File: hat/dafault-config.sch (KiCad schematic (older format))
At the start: 22 parts

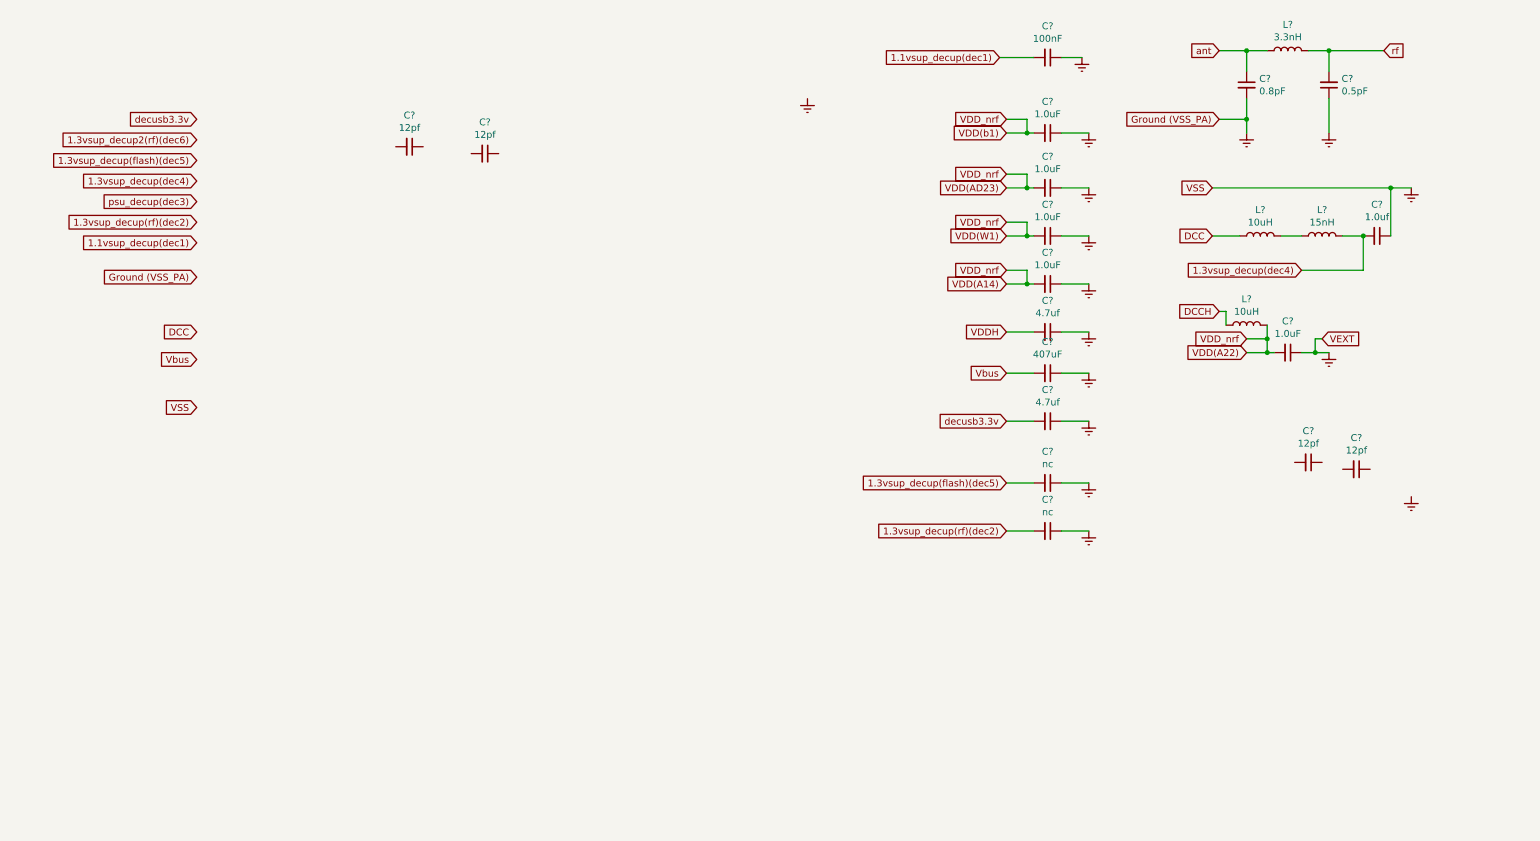
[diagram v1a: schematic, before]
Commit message: did some cleanup and added power connections
did some cleanup and added power connections
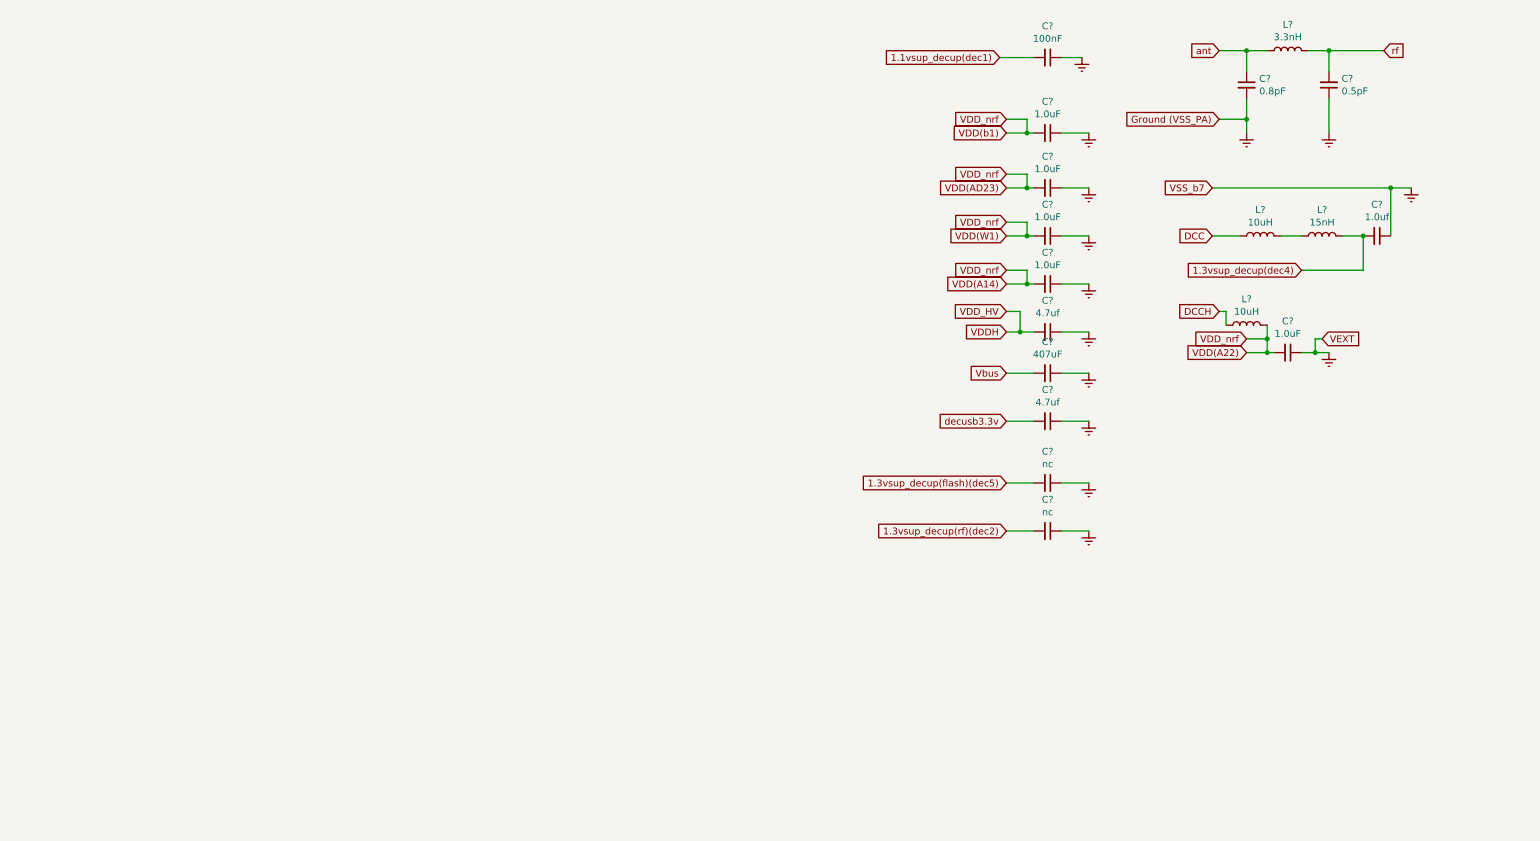
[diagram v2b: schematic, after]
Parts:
- removed C? (x4): 12pf, symbol Device:C_Small
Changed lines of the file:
@@
 Text GLabel 7900 1800 0    50   Input ~ 0
 VDD(AD23)
-Text GLabel 7900 2850 0    50   Input ~ 0
-VDDH
-Text GLabel 2000 3050 0    50   Input ~ 0
-Vbus
-Text GLabel 2000 2850 0    50   Input ~ 0
-DCC
+Text GLabel 7900 2700 0    50   Input ~ 0
+VDD_HV
 Text GLabel 9450 2700 0    50   Input ~ 0
 DCCH
-Text GLabel 2000 2450 0    50   Input ~ 0
-Ground (VSS_PA)
-Text GLabel 2000 2200 0    50   Input ~ 0
-1.1vsup_decup(dec1)
-Text GLabel 2000 2050 0    50   Input ~ 0
-1.3vsup_decup(rf)(dec2)
-Text GLabel 2000 1900 0    50   Input ~ 0
-psu_decup(dec3)
-Text GLabel 2000 1750 0    50   Input ~ 0
-1.3vsup_decup(dec4)
-Text GLabel 2000 1600 0    50   Input ~ 0
-1.3vsup_decup(flash)(dec5)
-Text GLabel 2000 1450 0    50   Input ~ 0
-1.3vsup_decup2(rf)(dec6)
-Text GLabel 2000 1300 0    50   Input ~ 0
-decusb3.3v
 $Comp
 L Device:C_Small C?
@@
 $Comp
 L Device:C_Small C?
-U 1 1 5CC155CD
-P 3550 1500
-AR Path="/5CC155CD" Ref="C?"  Part="1"
-AR Path="/5C9FDFE4/5CC155CD" Ref="C?"  Part="1"
-F 0 "C?" V 3321 1500 50  0000 C CNN
-F 1 "12pf" V 3412 1500 50  0000 C CNN
-F 2 "" H 3550 1500 50  0001 C CNN
-F 3 "~" H 3550 1500 50  0001 C CNN
-	1    3550 1500
-	0    1    1    0
-$EndComp
-$Comp
-L Device:C_Small C?
 U 1 1 5CC155E6
 P 8200 1400
@@
 F 3 "~" H 8200 1400 50  0001 C CNN
 	1    8200 1400
-	0    1    1    0
-$EndComp
-$Comp
-L Device:C_Small C?
-U 1 1 5CC155F4
-P 4100 1550
-AR Path="/5CC155F4" Ref="C?"  Part="1"
-AR Path="/5C9FDFE4/5CC155F4" Ref="C?"  Part="1"
-F 0 "C?" V 3871 1550 50  0000 C CNN
-F 1 "12pf" V 3962 1550 50  0000 C CNN
-F 2 "" H 4100 1550 50  0001 C CNN
-F 3 "~" H 4100 1550 50  0001 C CNN
-	1    4100 1550
 	0    1    1    0
 $EndComp
@@
 $Comp
 L Device:C_Small C?
-U 1 1 5CC1563E
-P 10100 3800
-AR Path="/5CC1563E" Ref="C?"  Part="1"
-AR Path="/5C9FDFE4/5CC1563E" Ref="C?"  Part="1"
-F 0 "C?" V 9871 3800 50  0000 C CNN
-F 1 "12pf" V 9962 3800 50  0000 C CNN
-F 2 "" H 10100 3800 50  0001 C CNN
-F 3 "~" H 10100 3800 50  0001 C CNN
-	1    10100 3800
-	0    1    1    0
-$EndComp
-$Comp
-L Device:C_Small C?
-U 1 1 5CC15651
-P 10450 3850
-AR Path="/5CC15651" Ref="C?"  Part="1"
-AR Path="/5C9FDFE4/5CC15651" Ref="C?"  Part="1"
-F 0 "C?" V 10221 3850 50  0000 C CNN
-F 1 "12pf" V 10312 3850 50  0000 C CNN
-F 2 "" H 10450 3850 50  0001 C CNN
-F 3 "~" H 10450 3850 50  0001 C CNN
-	1    10450 3850
-	0    1    1    0
-$EndComp
-$Comp
-L Device:C_Small C?
 U 1 1 5CC15663
 P 10600 2150
@@
 $EndComp
 $Comp
-L power:Earth #PWR?
+L power:Earth #PWR0101
 U 1 1 5CC15A29
 P 8450 850
-F 0 "#PWR?" H 8450 600 50  0001 C CNN
+F 0 "#PWR0101" H 8450 600 50  0001 C CNN
 F 1 "Earth" H 8450 700 50  0001 C CNN
 F 2 "" H 8450 850 50  0001 C CNN
@@
 $EndComp
 $Comp
-L power:Earth #PWR?
+L power:Earth #PWR0102
 U 1 1 5CC15A90
 P 8500 1400
-F 0 "#PWR?" H 8500 1150 50  0001 C CNN
+F 0 "#PWR0102" H 8500 1150 50  0001 C CNN
 F 1 "Earth" H 8500 1250 50  0001 C CNN
 F 2 "" H 8500 1400 50  0001 C CNN
@@
 $EndComp
 $Comp
-L power:Earth #PWR?
-U 1 1 5CC15AA4
-P 6450 1150
-F 0 "#PWR?" H 6450 900 50  0001 C CNN
-F 1 "Earth" H 6450 1000 50  0001 C CNN
-F 2 "" H 6450 1150 50  0001 C CNN
-F 3 "~" H 6450 1150 50  0001 C CNN
-	1    6450 1150
-	1    0    0    -1
-$EndComp
-$Comp
-L power:Earth #PWR?
+L power:Earth #PWR0104
 U 1 1 5CC15AB8
 P 8500 2850
-F 0 "#PWR?" H 8500 2600 50  0001 C CNN
+F 0 "#PWR0104" H 8500 2600 50  0001 C CNN
 F 1 "Earth" H 8500 2700 50  0001 C CNN
 F 2 "" H 8500 2850 50  0001 C CNN
@@
 $EndComp
 $Comp
-L power:Earth #PWR?
-U 1 1 5CC15ACC
-P 10850 4050
-F 0 "#PWR?" H 10850 3800 50  0001 C CNN
-F 1 "Earth" H 10850 3900 50  0001 C CNN
-F 2 "" H 10850 4050 50  0001 C CNN
-F 3 "~" H 10850 4050 50  0001 C CNN
-	1    10850 4050
-	1    0    0    -1
-$EndComp
-$Comp
-L power:Earth #PWR?
+L power:Earth #PWR0106
 U 1 1 5CC15AE0
 P 8500 4300
-F 0 "#PWR?" H 8500 4050 50  0001 C CNN
+F 0 "#PWR0106" H 8500 4050 50  0001 C CNN
 F 1 "Earth" H 8500 4150 50  0001 C CNN
 F 2 "" H 8500 4300 50  0001 C CNN
@@
 $EndComp
 $Comp
-L power:Earth #PWR?
+L power:Earth #PWR0107
 U 1 1 5CC15AF4
 P 10250 1400
-F 0 "#PWR?" H 10250 1150 50  0001 C CNN
+F 0 "#PWR0107" H 10250 1150 50  0001 C CNN
 F 1 "Earth" H 10250 1250 50  0001 C CNN
 F 2 "" H 10250 1400 50  0001 C CNN
@@
 $EndComp
 $Comp
-L power:Earth #PWR?
+L power:Earth #PWR0108
 U 1 1 5CC15B08
 P 10850 1800
-F 0 "#PWR?" H 10850 1550 50  0001 C CNN
+F 0 "#PWR0108" H 10850 1550 50  0001 C CNN
 F 1 "Earth" H 10850 1650 50  0001 C CNN
 F 2 "" H 10850 1800 50  0001 C CNN
@@
 $EndComp
 $Comp
-L power:Earth #PWR?
+L power:Earth #PWR0109
 U 1 1 5CC15B1C
 P 8500 3500
-F 0 "#PWR?" H 8500 3250 50  0001 C CNN
+F 0 "#PWR0109" H 8500 3250 50  0001 C CNN
 F 1 "Earth" H 8500 3350 50  0001 C CNN
 F 2 "" H 8500 3500 50  0001 C CNN
@@
 $EndComp
 $Comp
-L power:Earth #PWR?
+L power:Earth #PWR0110
 U 1 1 5CC15B30
 P 10250 3000
-F 0 "#PWR?" H 10250 2750 50  0001 C CNN
+F 0 "#PWR0110" H 10250 2750 50  0001 C CNN
 F 1 "Earth" H 10250 2850 50  0001 C CNN
 F 2 "" H 10250 3000 50  0001 C CNN
@@
 $EndComp
 $Comp
-L power:Earth #PWR?
+L power:Earth #PWR0111
 U 1 1 5CC15B44
 P 8500 2150
-F 0 "#PWR?" H 8500 1900 50  0001 C CNN
+F 0 "#PWR0111" H 8500 1900 50  0001 C CNN
 F 1 "Earth" H 8500 2000 50  0001 C CNN
 F 2 "" H 8500 2150 50  0001 C CNN
@@
 $EndComp
 $Comp
-L power:Earth #PWR?
+L power:Earth #PWR0112
 U 1 1 5CC15B58
 P 8500 1800
-F 0 "#PWR?" H 8500 1550 50  0001 C CNN
+F 0 "#PWR0112" H 8500 1550 50  0001 C CNN
 F 1 "Earth" H 8500 1650 50  0001 C CNN
 F 2 "" H 8500 1800 50  0001 C CNN
@@
 $EndComp
 $Comp
-L power:Earth #PWR?
+L power:Earth #PWR0113
 U 1 1 5CC15B6C
 P 8500 3150
-F 0 "#PWR?" H 8500 2900 50  0001 C CNN
+F 0 "#PWR0113" H 8500 2900 50  0001 C CNN
 F 1 "Earth" H 8500 3000 50  0001 C CNN
 F 2 "" H 8500 3150 50  0001 C CNN
@@
 $EndComp
 $Comp
-L power:Earth #PWR?
+L power:Earth #PWR0114
 U 1 1 5CC15B80
 P 9650 1400
-F 0 "#PWR?" H 9650 1150 50  0001 C CNN
+F 0 "#PWR0114" H 9650 1150 50  0001 C CNN
 F 1 "Earth" H 9650 1250 50  0001 C CNN
 F 2 "" H 9650 1400 50  0001 C CNN
@@
 $EndComp
 $Comp
-L power:Earth #PWR?
+L power:Earth #PWR0115
 U 1 1 5CC15B94
 P 8500 3950
-F 0 "#PWR?" H 8500 3700 50  0001 C CNN
+F 0 "#PWR0115" H 8500 3700 50  0001 C CNN
 F 1 "Earth" H 8500 3800 50  0001 C CNN
 F 2 "" H 8500 3950 50  0001 C CNN
@@
 Text GLabel 9400 2150 0    50   Input ~ 0
 DCC
-Text GLabel 2000 3400 0    50   Input ~ 0
-VSS
 Text GLabel 9400 1800 0    50   Input ~ 0
-VSS
+VSS_b7
 $Comp
 L Device:L L?
@@
 	8100 4300 7900 4300
 $Comp
-L power:Earth #PWR?
+L power:Earth #PWR0116
 U 1 1 5CC9F776
 P 8500 2500
-F 0 "#PWR?" H 8500 2250 50  0001 C CNN
+F 0 "#PWR0116" H 8500 2250 50  0001 C CNN
 F 1 "Earth" H 8500 2350 50  0001 C CNN
 F 2 "" H 8500 2500 50  0001 C CNN
@@
 	8300 2850 8500 2850
 Wire Wire Line
-	8100 2850 7900 2850
-Wire Wire Line
 	8300 3500 8500 3500
 Wire Wire Line
@@
 Wire Wire Line
 	8100 3500 7900 3500
+Text GLabel 7900 2850 0    50   Input ~ 0
+VDDH
+Wire Wire Line
+	8100 2850 8000 2850
+Wire Wire Line
+	7900 2700 8000 2700
+Wire Wire Line
+	8000 2700 8000 2850
+Connection ~ 8000 2850
+Wire Wire Line
+	8000 2850 7900 2850
 $EndSCHEMATC

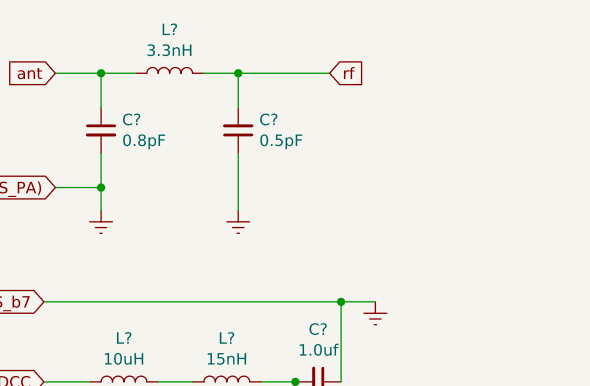
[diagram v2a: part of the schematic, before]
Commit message: added sma connector
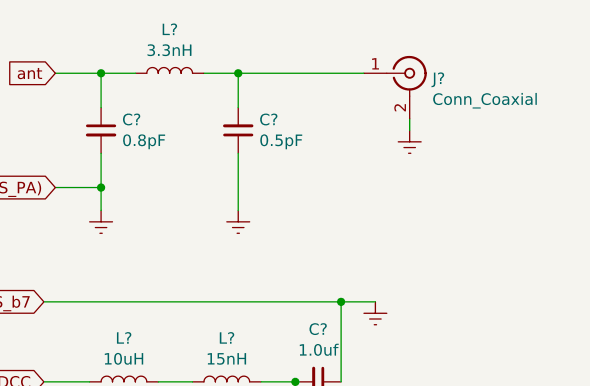
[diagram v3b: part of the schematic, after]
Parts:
- added J?: Conn_Coaxial, symbol Connector:Conn_Coaxial
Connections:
- net Earth: now also J?.2 (Ext)
- net rf: no longer names the net of C?.2, L?.2
- net rf: now also J?.1 (In)
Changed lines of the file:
@@
 Wire Wire Line
 	10250 800  10250 950
-Text GLabel 10650 800  2    50   Input ~ 0
-rf
-Wire Wire Line
-	10250 800  10650 800
 Connection ~ 10250 800
 Text GLabel 7900 3150 0    50   Input ~ 0
@@
 Wire Wire Line
 	8000 2850 7900 2850
+$Comp
+L Connector:Conn_Coaxial J?
+U 1 1 5C8668E2
+P 11000 800
+F 0 "J?" H 11099 776 50  0000 L CNN
+F 1 "Conn_Coaxial" H 11099 685 50  0000 L CNN
+F 2 "" H 11000 800 50  0001 C CNN
+F 3 " ~" H 11000 800 50  0001 C CNN
+	1    11000 800
+	1    0    0    -1
+$EndComp
+Wire Wire Line
+	10250 800  10800 800
+$Comp
+L power:Earth #PWR?
+U 1 1 5C8694A0
+P 11000 1050
+F 0 "#PWR?" H 11000 800 50  0001 C CNN
+F 1 "Earth" H 11000 900 50  0001 C CNN
+F 2 "" H 11000 1050 50  0001 C CNN
+F 3 "~" H 11000 1050 50  0001 C CNN
+	1    11000 1050
+	1    0    0    -1
+$EndComp
+Wire Wire Line
+	11000 1000 11000 1050
 $EndSCHEMATC

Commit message: added sma ufl connector
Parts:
- added ANT?: CONUFL001-SMD, CONUFL001-SMD, symbol SamacSys_Parts:CONUFL001-SMD
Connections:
- wire segments 65 -> 75
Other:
- moved on the sheet: C?, J?, L?
